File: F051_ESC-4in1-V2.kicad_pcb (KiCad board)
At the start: 4 copper layers, 46 x 55.8 mm, 223 parts, among them J1 Conn_01x02, J10 Conn_01x03, J11 Conn_01x03, J2 Conn_01x10, J3 Conn_01x05, J4 Conn_01x05, J5 Conn_01x05, J6 Conn_01x03, J7 Conn_01x05, J8 Conn_01x03, J9 Conn_01x10, Q1 TPH1R204PB, Q10 TPH1R204PB, Q11 TPH1R204PB, Q12 TPH1R204PB, Q13 TPH1R204PB, Q14 TPH1R204PB, Q15 TPH1R204PB, Q16 TPH1R204PB, Q17 TPH1R204PB, Q18 TPH1R204PB, Q19 TPH1R204PB, Q2 TPH1R204PB, Q20 TPH1R204PB, Q21 TPH1R204PB, Q22 TPH1R204PB, Q23 TPH1R204PB, Q24 TPH1R204PB, Q3 TPH1R204PB, Q4 TPH1R204PB, Q5 TPH1R204PB, Q6 TPH1R204PB, Q7 TPH1R204PB, Q8 TPH1R204PB, Q9 TPH1R204PB, U1 FD6288Q, U10 FD6288Q, U11 FD6288Q, U12 STM32F051K6Ux, U13 L78L12_SOT89, U14 MP4560_QFN10, U2 STM32F051K6Ux, U3 L78L12_SOT89, U4 LP2985-3.3, U5 INA139, U6 STM32F051K6Ux, U7 OPA340NA, U8 FD6288Q, U9 STM32F051K6Ux

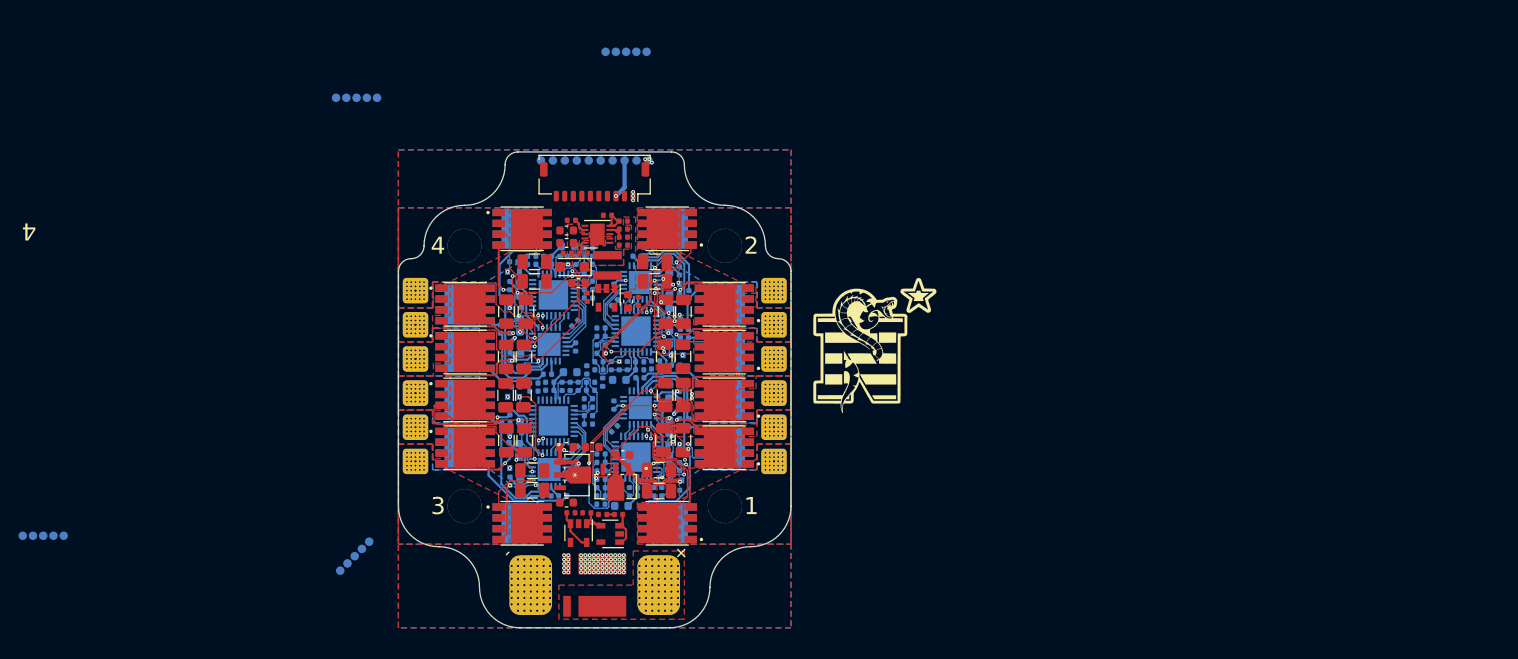
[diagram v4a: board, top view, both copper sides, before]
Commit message: Lots of routing done to get rid of no-connects.  Down to 35 or so
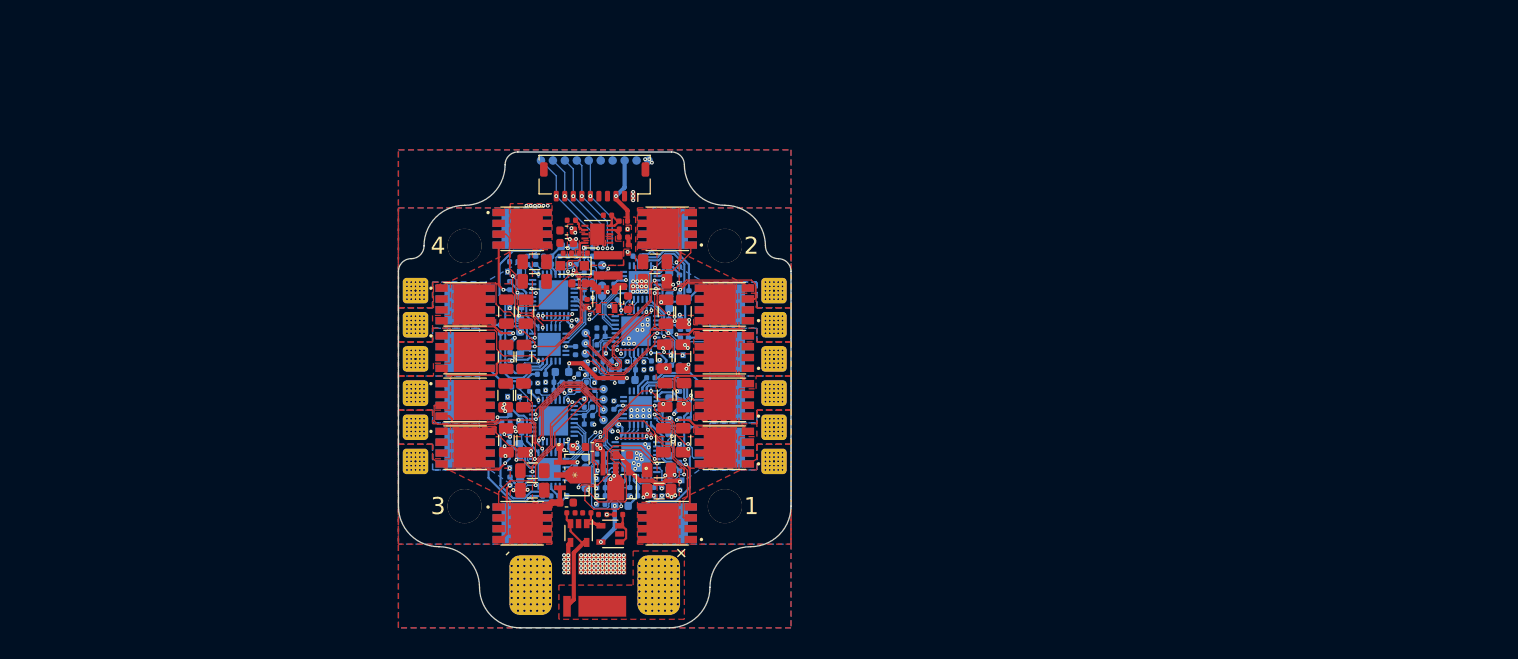
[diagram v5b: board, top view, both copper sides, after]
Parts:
- removed G***: LOGO, Footprints:DTOM_L
- J3, J4, J5, J7: value Conn_01x05 -> Conn_01x04
- moved J5 67.2 mm to (138.9, 85.3), turned to 270 degrees
- moved J3 49.5 mm to (138.9, 99.8), turned to 270 degrees
- moved J7 35.9 mm to (140.9, 77.3), turned to 90 degrees
- moved J4 34.1 mm to (141.0, 91.8), turned to 90 degrees
- moved C23 6.01 mm to (139.1, 80.0)
- moved C22 5.02 mm to (144.0, 78.0), turned to 0 degrees
- moved R12 1.28 mm to (146.6, 88.7)
- moved FB2 1.05 mm to (143.9, 89.0)
- moved FB3 0.95 mm to (136.2, 88.0)
- moved R25 0.77 mm to (141.5, 88.7), turned to 180 degrees
- moved R77 0.75 mm to (143.9, 73.6), turned to 270 degrees
- moved R42 0.70 mm to (138.6, 88.3), turned to 0 degrees
- moved R60 0.70 mm to (133.8, 88.3)
- moved C47 0.68 mm to (132.1, 75.0), turned to 90 degrees
- moved C34 0.68 mm to (132.4, 89.8), turned to 90 degrees
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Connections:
- J3 pad 3: /MCU_1/NRST -> /MCU_1/USART1_TX
- J4 pad 1: /MCU 3/SWCLK -> /MCU 3/SWDIO
- J4 pad 2: /MCU 3/SWDIO -> /MCU 3/SWCLK
- J4 pad 3: /MCU 3/NRST -> /MCU 3/USART1_TX
- J5 pad 1: /MCU_2/SWCLK -> /MCU_2/SWDIO
- J5 pad 2: /MCU_2/SWDIO -> /MCU_2/SWCLK
- J5 pad 3: /MCU_2/NRST -> /MCU_2/USART1_TX
- J7 pad 3: /MCU_4/NRST -> /MCU_4/USART1_TX
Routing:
- net +3V3: track 10.3 -> 94.7 mm, vias 0 -> 14
- net /Curent Sense/CURR: track 0.89 -> 45.3 mm, vias 0 -> 3
- net /PWM_1: track 0.00 -> 43.0 mm, vias 0 -> 3
- net /PWM_2: track 0.00 -> 30.9 mm, vias 0 -> 3
- net /PWM_3: track 0.00 -> 29.2 mm, vias 0 -> 3
- net /MCU_1/USART1_RX: track 0.00 -> 18.5 mm, vias 1 -> 2
- net /MCU 3/PhaseC: track 10.8 -> 26.0 mm, vias 25 -> 26
- net /MCU_2/SWDIO: track 0.24 -> 14.8 mm, vias 1 -> 2
- net /MCU_2/SWCLK: track 0.06 -> 14.5 mm, vias 1 -> 2
- net /MCU 3/SWDIO: track 0.00 -> 13.7 mm, vias 1 -> 2
- net /MCU 3/SWCLK: track 0.06 -> 13.5 mm, vias 1 -> 2
- net /PWM_4: track 0.00 -> 12.7 mm, vias 0 -> 1
- net /MCU_2/PhaseB: track 16.1 -> 28.7 mm
- net /MCU_1/USART1_TX: track 2.70 -> 14.9 mm, vias 1 -> 2
- net /MCU_2/USART1_TX: track 0.00 -> 12.0 mm, vias 0 -> 2
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- added copper zone on F.Cu, net +3V3
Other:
- board text removed: "TX"

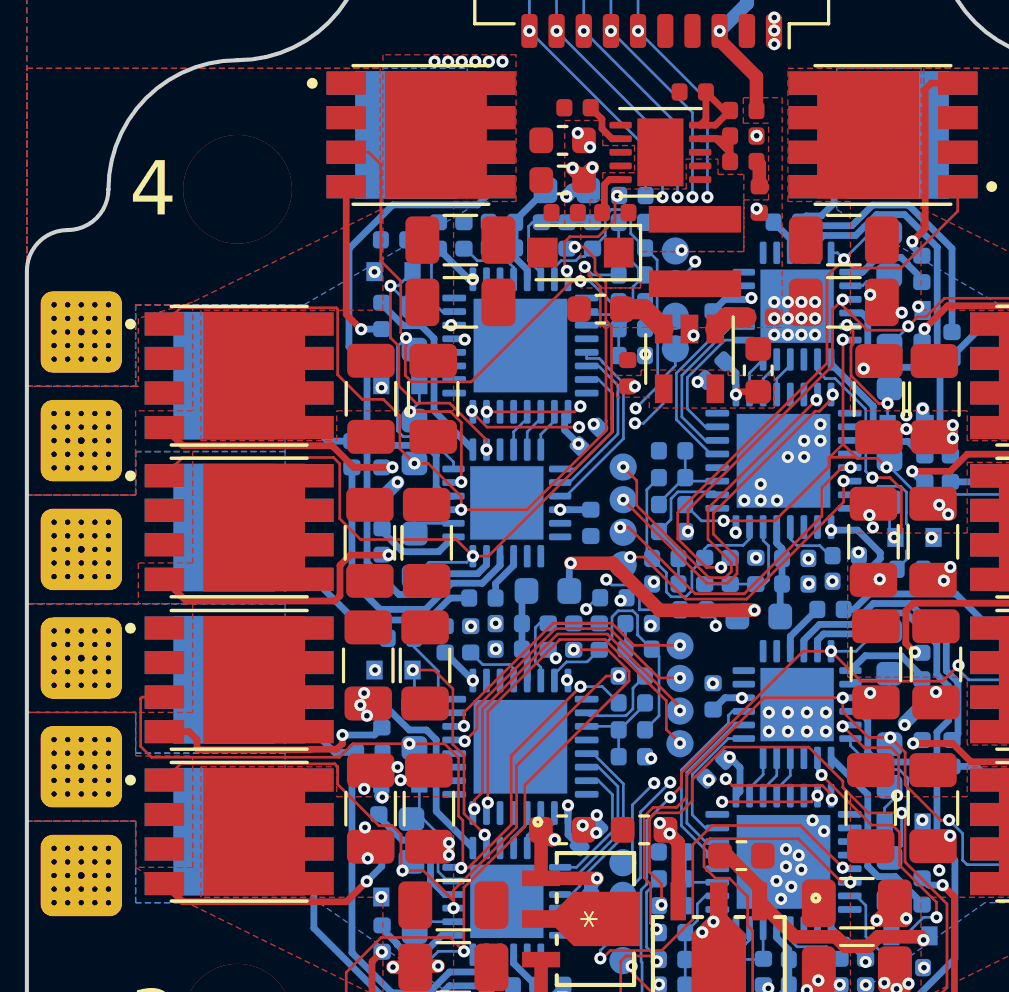
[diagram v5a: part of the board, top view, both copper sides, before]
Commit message: More traces routed.  Down to 11 no-connects
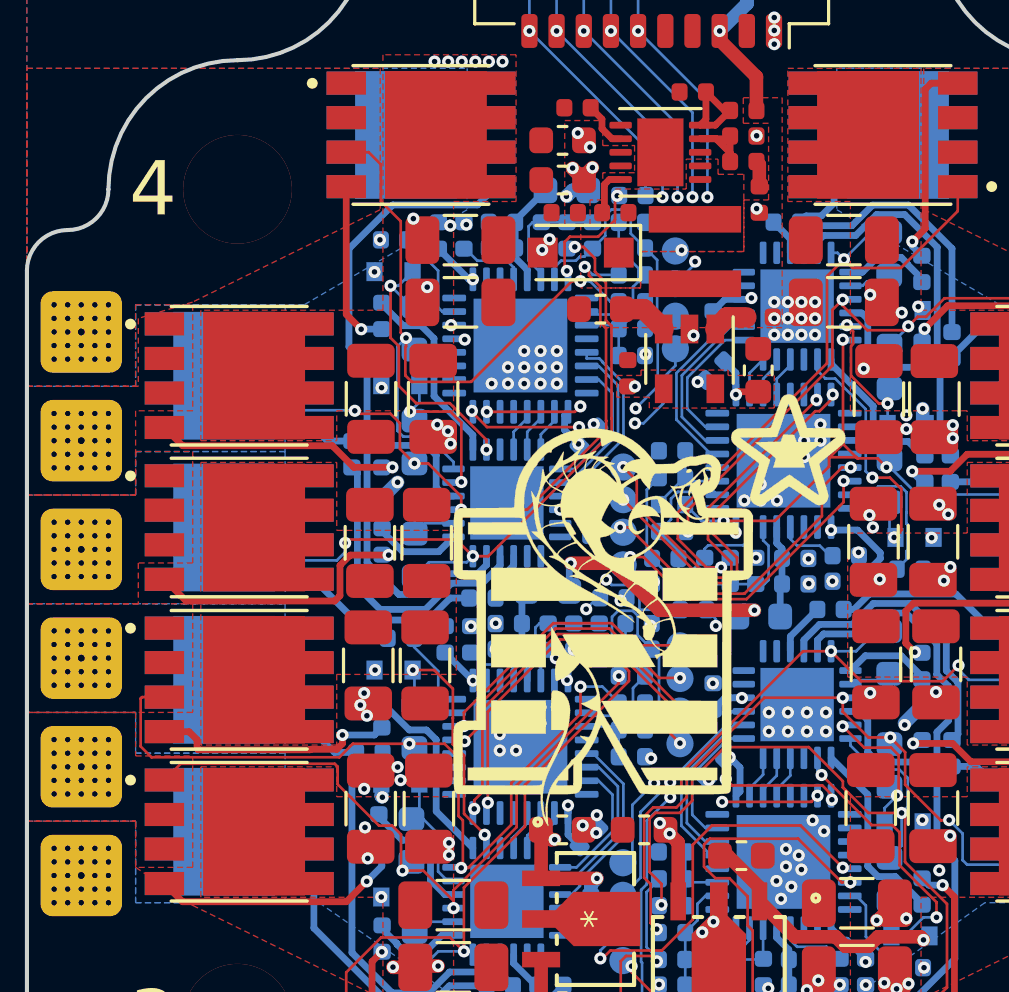
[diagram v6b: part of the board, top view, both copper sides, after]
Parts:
- added G***: LOGO, Footprints:DTOM_L, F.Cu at (139.7, 88.6)
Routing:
- net /MCU_4/PhaseB: track 32.3 -> 27.3 mm, vias 28 -> 29
- net /MCU_4/PhaseC: track 33.1 -> 29.2 mm, vias 27 -> 28
- net GND: track 1.03 -> 1.52 mm, vias 144 -> 171
- net VCC_Shunt: vias 102 -> 104

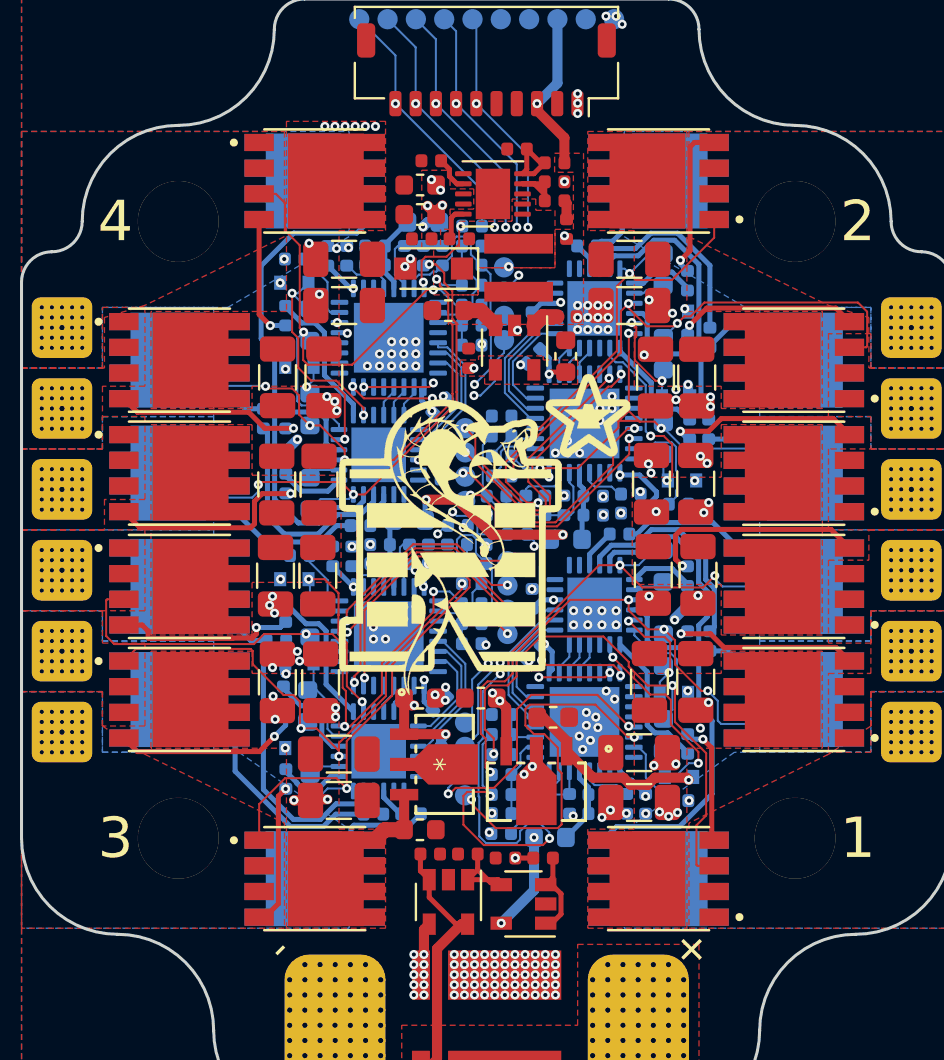
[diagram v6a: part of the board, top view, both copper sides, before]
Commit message: Finished routing all traces
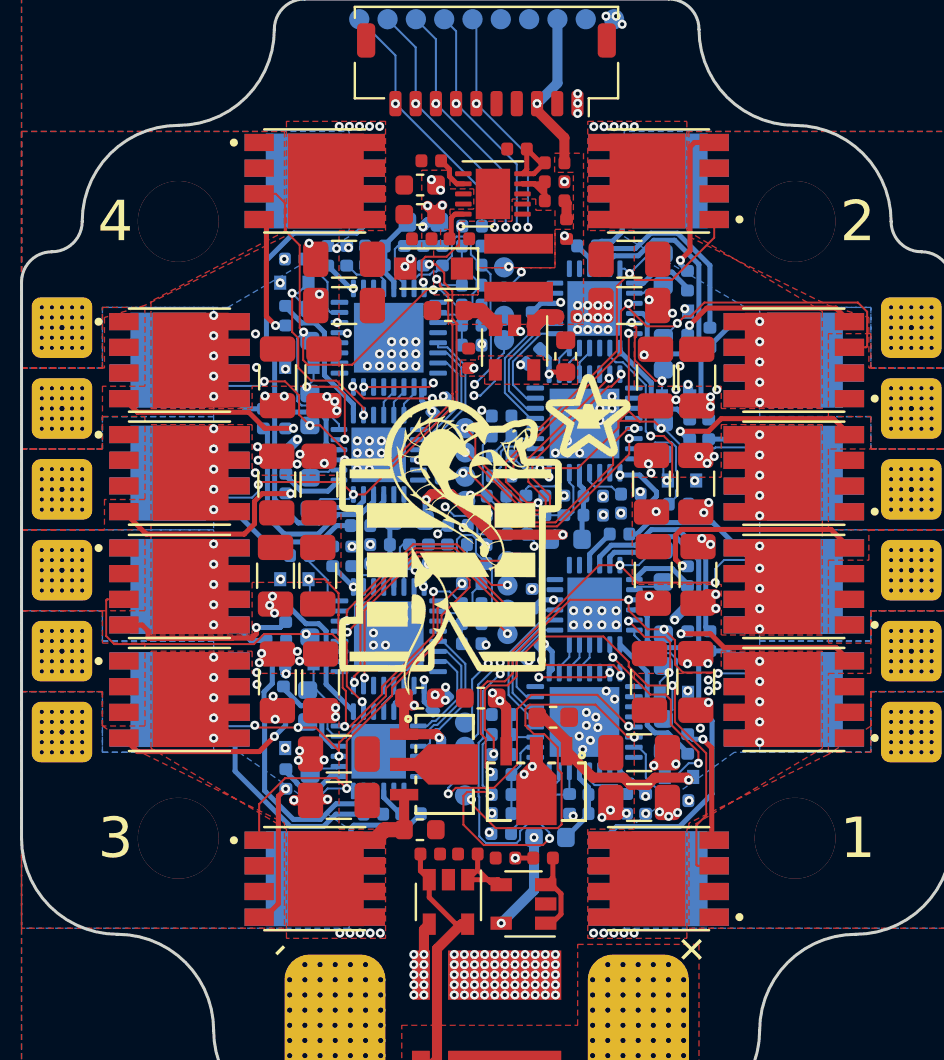
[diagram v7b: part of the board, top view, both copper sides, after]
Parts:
- moved C37 0.24 mm to (137.8, 100.0)
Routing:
- net /MCU 3/PhaseB: track 26.8 -> 23.0 mm, vias 27 -> 28
- net GND: track 1.52 -> 3.57 mm, vias 171 -> 201
- net /MOSFET_Driver_4/VB3: track 4.58 -> 2.95 mm
- net /MCU_1/PhaseB: track 28.4 -> 27.0 mm
- net /MCU_1/PhaseC: track 34.0 -> 34.7 mm
- net +12V_1: track 26.2 -> 25.5 mm
- net /PWM_3: track 29.2 -> 29.7 mm
- net VCC_Shunt: vias 104 -> 164
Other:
- board text added: "TX"

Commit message: Finished adding vias and routing.  Under review
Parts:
- moved G*** 0.63 mm to (140.1, 89.1)
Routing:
- net +12V_2: track 31.2 -> 35.0 mm
- net +12V_1: track 25.5 -> 28.4 mm
- net GND: track 3.57 -> 4.14 mm, vias 201 -> 174
- net /MCU_4/PhaseB: track 27.5 -> 27.7 mm, vias 29 -> 17
- net /MCU_1/PhaseA: track 33.1 -> 33.3 mm, vias 27 -> 15
- net /MCU_2/PhaseA: vias 28 -> 16
- net /MCU_4/PhaseA: vias 27 -> 15
- net VCC_Shunt: vias 164 -> 133
- net VCC: vias 58 -> 31
- net /MCU_4/PhaseC: vias 28 -> 16
- net /MCU_2/PhaseC: vias 27 -> 15
- net /MCU_2/PhaseB: vias 28 -> 16
- net /MCU_1/PhaseC: vias 28 -> 16
- net /MCU_1/PhaseB: vias 29 -> 17
- net /MCU 3/PhaseC: vias 26 -> 15
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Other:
- board text added: "NC"
- board text removed: "NRST"
